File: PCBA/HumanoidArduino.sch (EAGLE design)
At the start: 8 parts, among them J1 22-27-2061-06, J2 22-27-2041-04, J3 22-27-2031-03

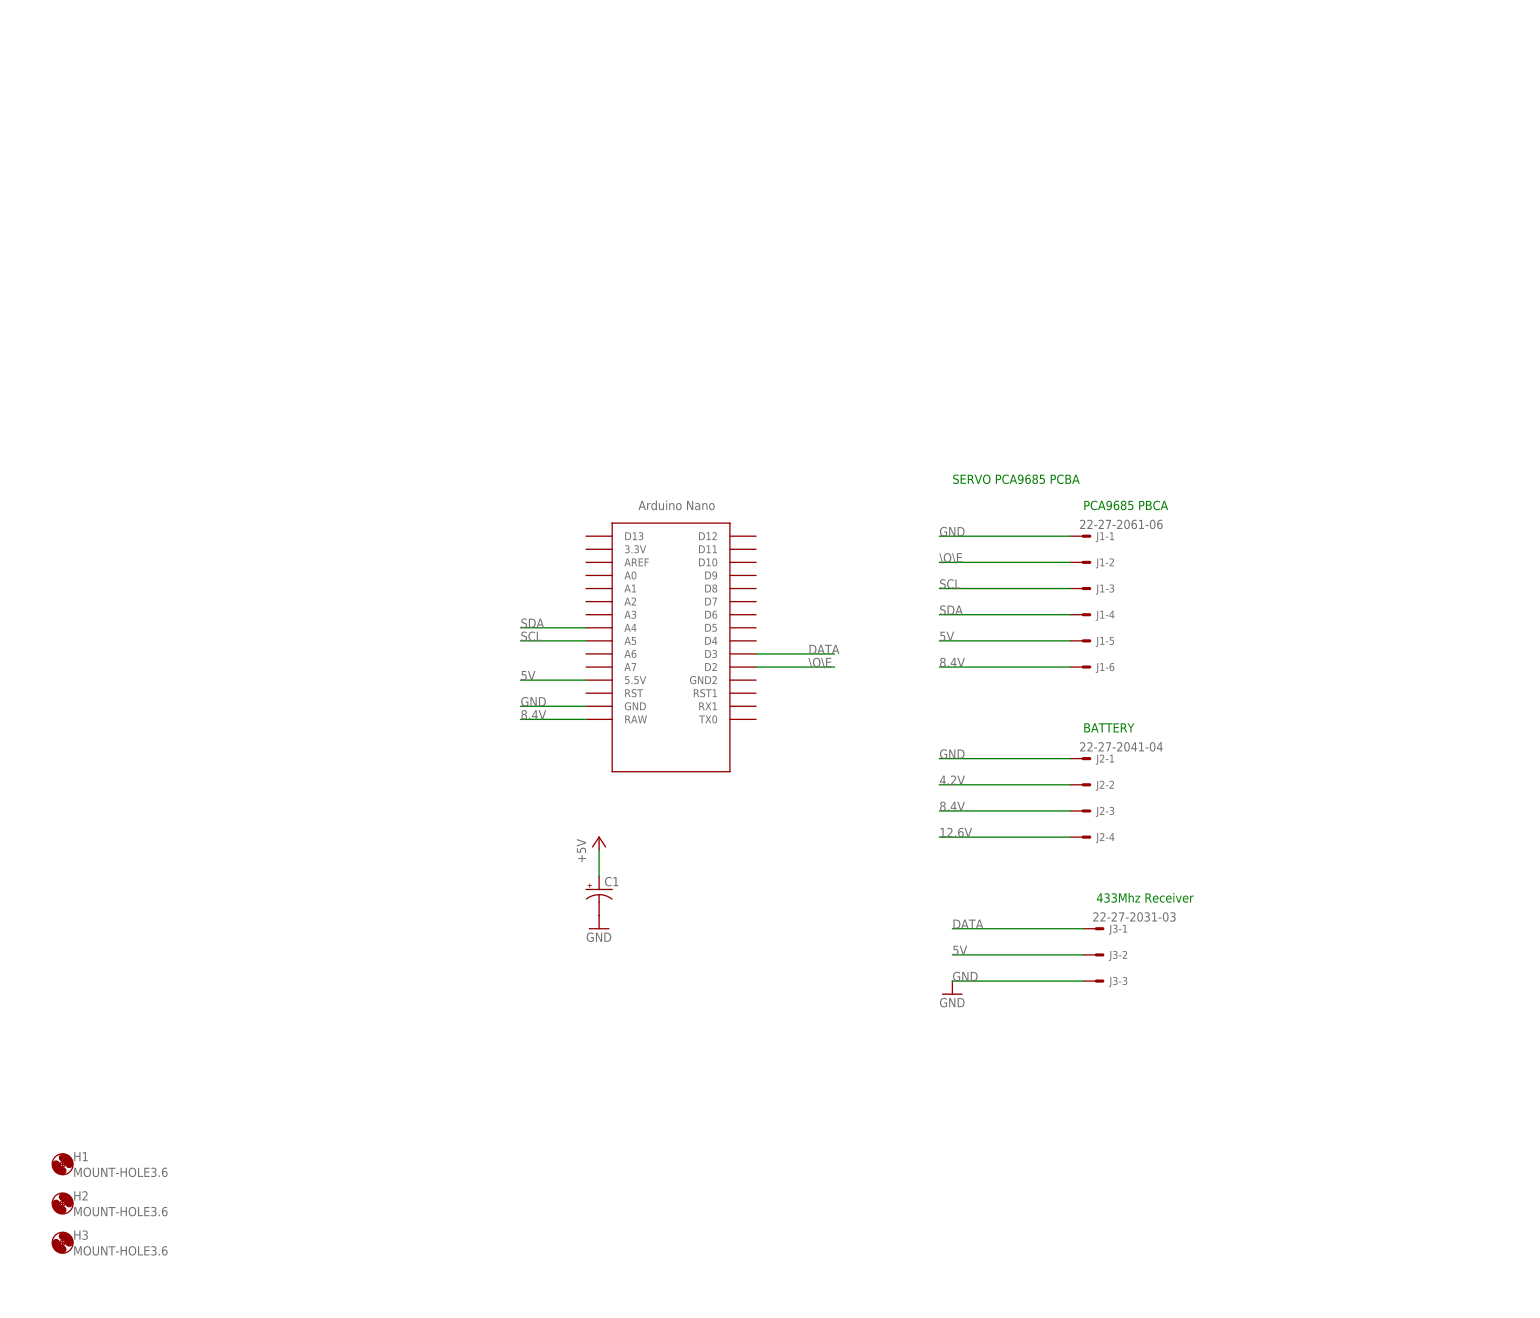
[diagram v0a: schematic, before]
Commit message: Replaces Arduino w. CHIP
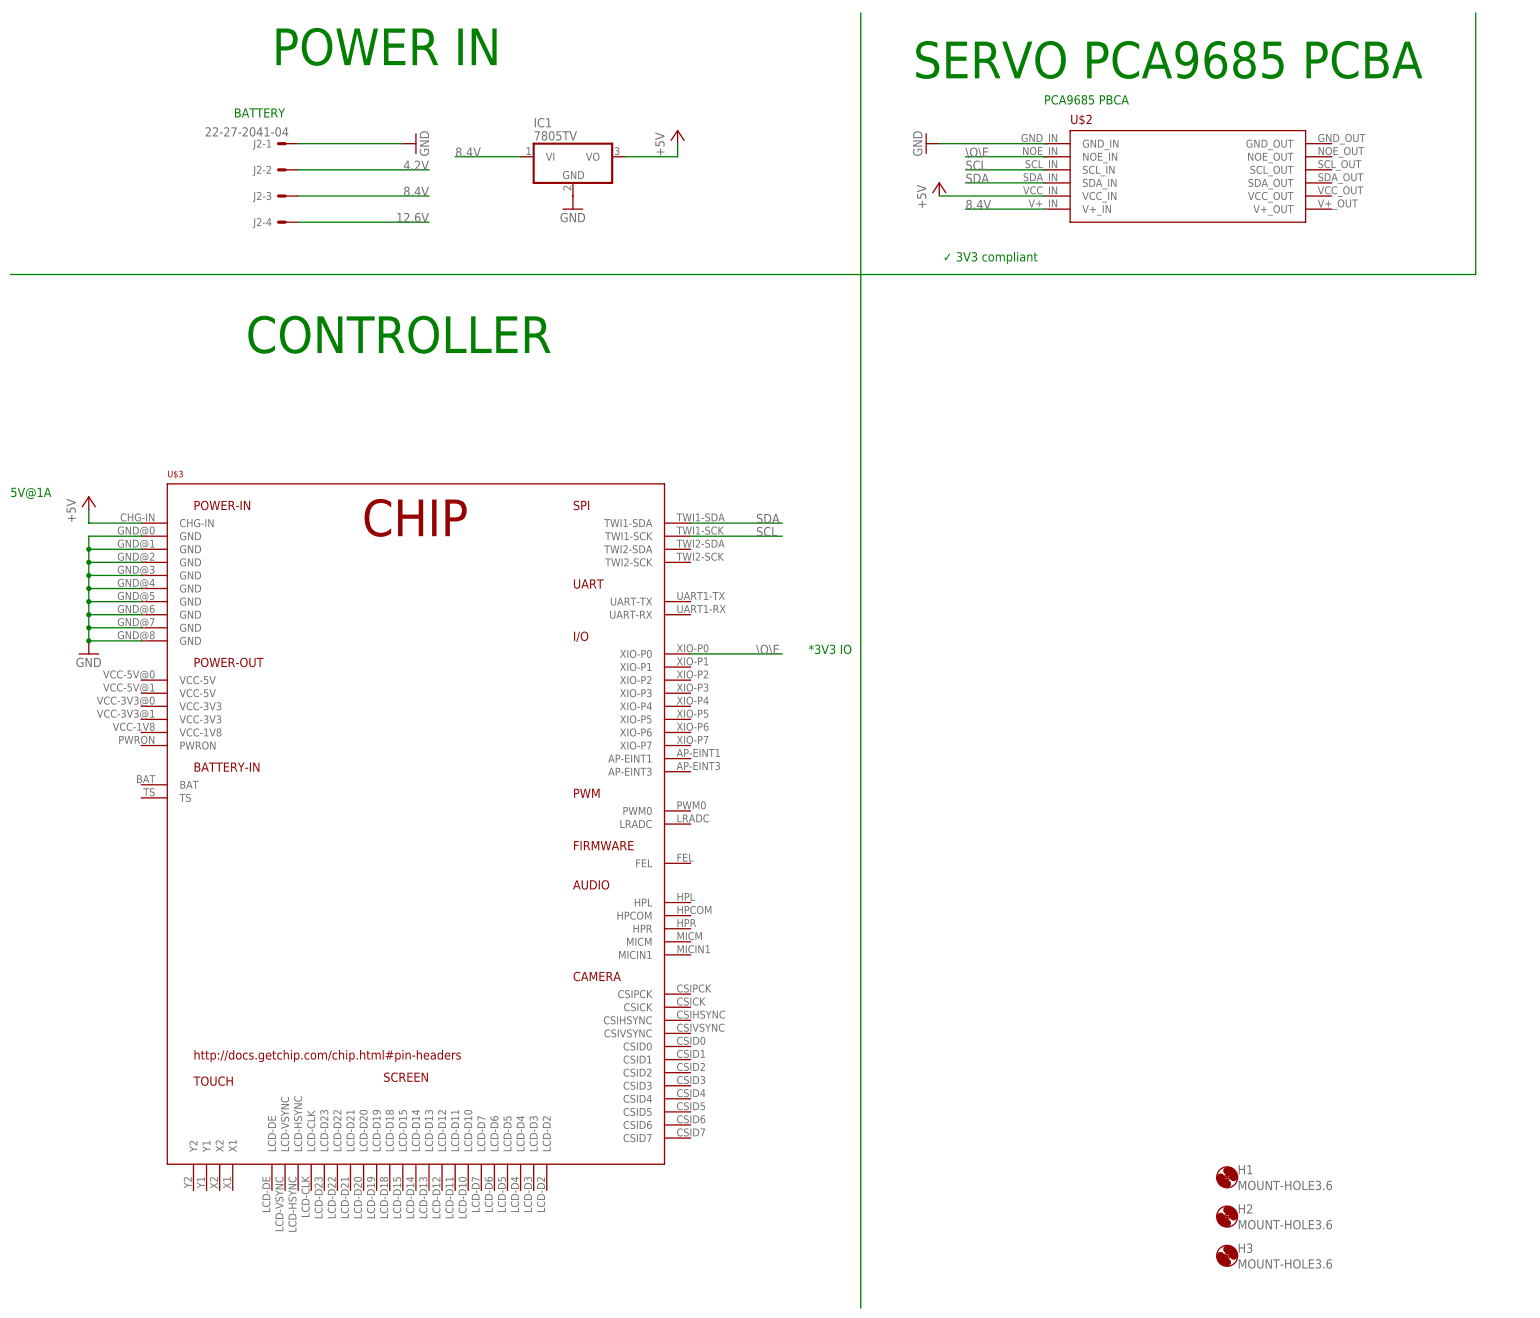
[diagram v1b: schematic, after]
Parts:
- removed C1: (no value), adafruit:CPOL-USE10-20
- removed J1: 22-27-2061-06, con-molex:22-27-2061-06
- removed J3: 22-27-2031-03, con-molex:22-27-2031-03
- removed U$1: NANO, Arduino-clone:NANO
- added IC1: 7805TV, linear:7805TV
- added U$2: ADAFRUIT_PCA9685, ZMZE:ADAFRUIT_PCA9685
- added U$3: CHIP, ZMZE:CHIP
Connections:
- removed net 5V: C1.+, J1-5.S, J3-2.S, U$1.5.5V
- removed net DATA: J3-1.S
- new net +5V: IC1.VO, U$2.VCC_IN, U$3.CHG-IN
- net 8.4V: now also IC1.VI, U$2.V+_IN; no longer J1-6.S, U$1.RAW
- net GND: now also IC1.GND, U$2.GND_IN, U$3.GND@0, U$3.GND@1, U$3.GND@2, U$3.GND@3, U$3.GND@4, U$3.GND@5, U$3.GND@6, U$3.GND@7, U$3.GND@8; no longer C1.-, J1-1.S, J3-3.S, U$1.GND
- net SCL: now also U$2.SCL_IN, U$3.TWI1-SCK; no longer J1-3.S, U$1.A5
- net SDA: now also U$2.SDA_IN, U$3.TWI1-SDA; no longer J1-4.S, U$1.A4
- net \O\E: now also U$2.NOE_IN, U$3.XIO-P0; no longer J1-2.S, U$1.D2
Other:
- note added: "*3V3 IO"
- note added: "5V@1A"
- note added: "CONTROLLER"
- note added: "POWER IN"
- note added: "￼ ✓ 3V3 compliant"
- note removed: "433Mhz Receiver"
- moved on the sheet: H1, H2, H3, J2-1, J2-2, J2-3, J2-4
